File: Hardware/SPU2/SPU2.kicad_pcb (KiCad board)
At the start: 2 copper layers, 400 x 300 mm, 736 parts, among them J1 Conn_Coaxial, J2 Conn_02x13_Counter_Clockwise, J3 Conn_01x02, J4 Conn_01x04_Male, Q2 BC547, Q3 BC547, Q4 BC547, SW1 SW_Push, SW2 SW_SPDT, SW3 SW_DIP_x02, U1 74LS86, U10 74LS08, U11 74LS173, U12 74LS173, U13 74LS161, U14 74LS161, U15 74LS161, U16 74LS173, U17 74LS173, U18 NE555, U19 74LS173, U2 74LS86, U20 74LS173, U21 74LS173, U22 74LS173, U23 74LS173, U24 74LS173, U25 74LS245, U26 M84Z02, U27 M84Z02, U28 74LS245, U29 74LS00, U3 74LS245, U30 28c64, U31 28c64, U32 74LS245, U33 74LS245, U34 74LS245, U35 74LS245, U36 74LS245, U37 74LS08, U38 74HCT574, U39 74HCT574, U4 74LS283, U40 74LS161, U41 74LS04, U42 74LS08, U43 NE555, U44 NE555, U45 74HCT574, U46 74HCT574, U47 74HCT574, U48 74HCT574, U49 74HCT574, U5 74LS283, U50 74HCT574, U51 74HCT574, U52 74HCT574, U53 74HCT574, U54 74HCT574, U55 74HCT574, U56 74HCT574, U57 74HCT574, U58 74HCT574, U59 74HCT574, U6 4077, U60 74HCT574, U61 INTEL2716, U62 74LS08, U63 INTEL2716, U64 74LS08, U65 74LS08, U66 74LS08, U67 74LS08, U68 INTEL2716, U69 CD4514B, U7 4077, U70 74LS157, U71 74LS245, U72 74LS245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

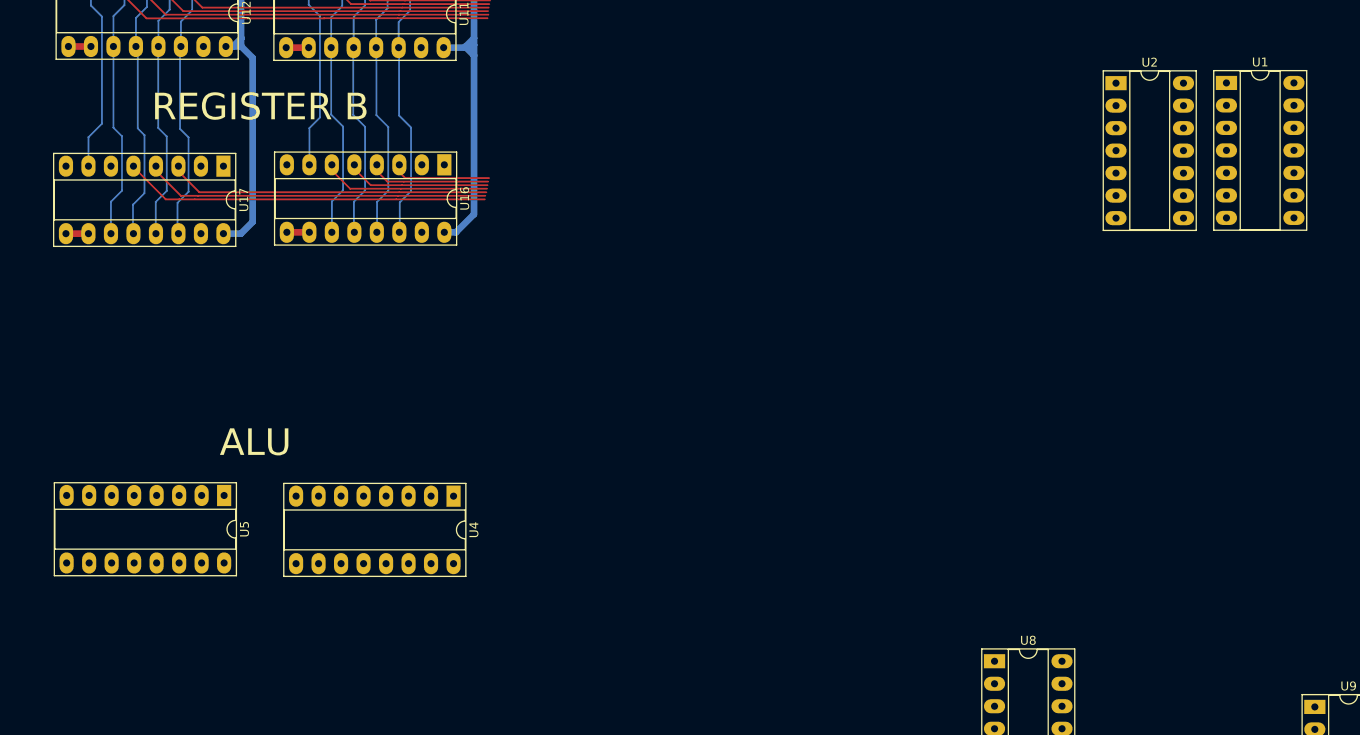
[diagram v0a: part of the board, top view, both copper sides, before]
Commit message: added subtraction to Reg B
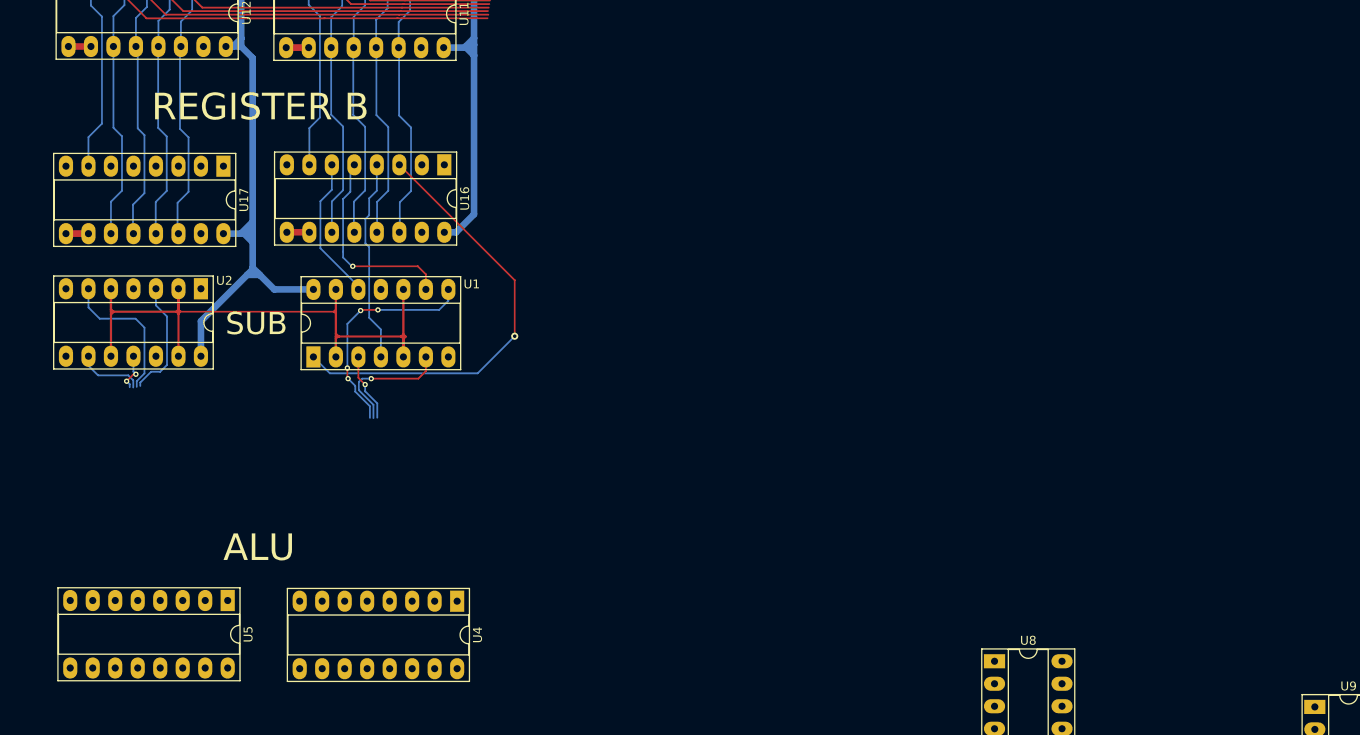
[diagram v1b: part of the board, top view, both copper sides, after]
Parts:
- moved U1 107.6 mm to (162.2, 201.0), turned to 90 degrees
- moved U2 105.9 mm to (149.5, 193.3), turned to 270 degrees
- moved U5 11.9 mm to (152.6, 228.5)
- moved U4 11.9 mm to (178.5, 228.6)
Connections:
- U1 pad 1: /REGB7 -> /REGB0
- U1 pad 11: /BAI1 -> /BAI3
- U1 pad 12: /REGB1 -> /REGB3
- U1 pad 3: /BAI7 -> /BAI0
- U1 pad 4: /REGB5 -> /REGB1
- U1 pad 6: /BAI5 -> /BAI1
- U1 pad 8: /BAI3 -> /BAI2
- U1 pad 9: /REGB3 -> /REGB2
- U2 pad 1: /REGB6 -> /REGB4
- U2 pad 11: /BAI0 -> /BAI7
- U2 pad 12: /REGB0 -> /REGB7
- U2 pad 3: /BAI6 -> /BAI4
- U2 pad 4: /REGB4 -> /REGB5
- U2 pad 6: /BAI4 -> /BAI5
- U2 pad 8: /BAI2 -> /BAI6
- U2 pad 9: /REGB2 -> /REGB6
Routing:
- net SU: track 0.00 -> 78.7 mm
- net /REGB5: track 38.9 -> 0.00 mm
- net /REGB0: track 11.2 -> 50.0 mm, vias 0 -> 1
- net /REGB4: track 36.5 -> 0.00 mm
- net /REGB6: track 41.3 -> 7.62 mm
- net +5V: track 1964.9 -> 1995.4 mm
- net /BAI2: track 0.00 -> 25.4 mm, vias 0 -> 4
- net /BAI5: track 0.00 -> 16.4 mm
- net /BAI1: track 0.00 -> 14.4 mm, vias 0 -> 1
- net /BAI4: track 0.00 -> 13.3 mm
- net /REGB1: track 13.8 -> 23.0 mm
- net /BAI0: track 0.00 -> 7.74 mm, vias 0 -> 1
- net /REGB2: track 16.3 -> 22.8 mm, vias 0 -> 1
- net /BAI7: track 0.00 -> 4.36 mm, vias 0 -> 2
- net /REGB3: track 19.0 -> 16.4 mm
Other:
- board text added: "SUB"

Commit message: schule aus
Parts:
- moved U4 15.5 mm to (177.5, 213.2)
- moved U5 15.4 mm to (152.3, 213.2)
- moved U1 0.36 mm to (161.9, 201.0)
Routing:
- net /RA5: track 39.2 -> 95.6 mm
- net /RA4: track 36.6 -> 91.8 mm
- net /RA6: track 41.9 -> 93.1 mm
- net /RA7: track 44.5 -> 86.5 mm
- net /RA3: track 19.2 -> 60.5 mm
- net SU: track 78.7 -> 115.9 mm
- net /BAI3: track 0.00 -> 33.5 mm, vias 0 -> 4
- net /BAI6: track 0.00 -> 32.9 mm, vias 0 -> 1
- net ~BI: track 5.08 -> 31.1 mm
- net /REGB7: track 0.00 -> 24.9 mm, vias 0 -> 2
- net /BAI2: track 25.4 -> 47.2 mm, vias 4 -> 5
- net /REGB6: track 7.62 -> 25.8 mm
- net /BAI7: track 4.36 -> 20.8 mm, vias 2 -> 0
- net /REGB4: track 0.00 -> 15.9 mm
- net /RA0: track 11.2 -> 26.7 mm, vias 0 -> 1
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
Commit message: began clusterfuck
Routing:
- net /RA1: track 26.9 -> 60.3 mm
- net /RA2: track 27.5 -> 60.7 mm
- net /RA0: track 26.7 -> 59.8 mm
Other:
- board size 400 x 300 mm -> 624.6 x 303.9 mm
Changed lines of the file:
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@@
-(kicad_pcb (version 20171130) (host pcbnew "(5.1.6)-1")
+(kicad_pcb (version 20171130) (host pcbnew "(5.1.4)-1")
   (general
     (thickness 1.6)
-    (drawings 27)
-    (tracks 5190)
+    (drawings 33)
+    (tracks 5200)
     (zones 0)
     (modules 736)
@@
   )
   (setup
-    (last_trace_width 0.2)
+    (last_trace_width 0.25)
     (user_trace_width 0.2)
     (user_trace_width 0.5)
@@
     )
   )
+  (gr_line (start 450.46 25.55) (end 458.1 21.88) (layer Edge.Cuts) (width 0.05))
+  (gr_line (start 445.36 294.77) (end 450.46 25.55) (layer Edge.Cuts) (width 0.05))
+  (gr_line (start 614.64 290.1) (end 445.36 294.77) (layer Edge.Cuts) (width 0.05))
+  (gr_line (start 664.61 177.34) (end 614.64 290.1) (layer Edge.Cuts) (width 0.05))
+  (gr_line (start 575.89 16.09) (end 664.61 177.34) (layer Edge.Cuts) (width 0.05))
+  (gr_line (start 458.1 21.88) (end 575.89 16.09) (layer Edge.Cuts) (width 0.05))
   (gr_text "SUB\n" (at 155.8036 196.9262) (layer F.SilkS)
     (effects (font (size 2.5 2.5) (thickness 0.3)))
@@
   (segment (start 171.8564 158.496) (end 171.8564 161.7726) (width 0.2) (layer B.Cu) (net 308))
   (segment (start 171.8564 161.7726) (end 171.0944 162.5346) (width 0.2) (layer B.Cu) (net 308))
-  (segment (start 171.0944 162.5346) (end 169.91993 163.70907) (width 0.2) (layer F.Cu) (net 308))
-  (segment (start 169.91993 163.70907) (end 169.9006 163.7284) (width 0.2) (layer F.Cu) (net 308))
+  (segment (start 137.54907 163.70907) (end 137.11 163.70907) (width 0.2) (layer F.Cu) (net 308))
+  (segment (start 160.48327 163.70907) (end 137.54907 163.70907) (width 0.2) (layer F.Cu) (net 308))
+  (segment (start 160.5026 163.7284) (end 160.48327 163.70907) (width 0.2) (layer F.Cu) (net 308))
+  (segment (start 171.0944 162.5346) (end 169.9006 163.7284) (width 0.2) (layer F.Cu) (net 308))
   (segment (start 169.9006 163.7284) (end 160.5026 163.7284) (width 0.2) (layer F.Cu) (net 308))
+  (segment (start 137.11 163.70907) (end 131.690418 163.70907) (width 0.2) (layer F.Cu) (net 308))
+  (segment (start 131.690418 163.70907) (end 128.885671 166.513817) (width 0.2) (layer F.Cu) (net 308))
+  (segment (start 128.885671 166.513817) (end 128.885671 166.84) (width 0.2) (layer F.Cu) (net 308))
   (segment (start 169.3164 158.496) (end 169.3164 159.1818) (width 0.2) (layer F.Cu) (net 309))
   (segment (start 169.3164 159.1818) (end 170.530611 160.396011) (width 0.2) (layer F.Cu) (net 309))
@@
   (segment (start 168.402 162.4584) (end 167.55134 163.30906) (width 0.2) (layer F.Cu) (net 309))
   (segment (start 167.55134 163.30906) (end 160.18534 163.30906) (width 0.2) (layer F.Cu) (net 309))
+  (segment (start 160.18534 163.30906) (end 131.52473 163.30906) (width 0.2) (layer F.Cu) (net 309))
+  (segment (start 131.52473 163.30906) (end 128.485661 166.348129) (width 0.2) (layer F.Cu) (net 309))
+  (segment (start 128.485661 166.348129) (end 128.485661 166.77) (width 0.2) (layer F.Cu) (net 309))
   (segment (start 166.7764 158.496) (end 166.7764 158.9278) (width 0.2) (layer F.Cu) (net 310))
   (segment (start 168.644621 160.796021) (end 172.567823 160.796021) (width 0.2) (layer F.Cu) (net 310))
   (segment (start 166.7764 158.9278) (end 168.644621 160.796021) (width 0.2) (layer F.Cu) (net 310))
   (segment (start 172.567823 160.796021) (end 182.1688 160.796021) (width 0.2) (layer F.Cu) (net 310))
-  (via (at 165.8366 162.306) (size 0.6) (drill 0.3) (layers F.Cu B.Cu) (net 310))
   (segment (start 166.7764 158.496) (end 166.7764 161.3662) (width 0.2) (layer B.Cu) (net 310))
   (segment (start 166.7764 161.3662) (end 165.8366 162.306) (width 0.2) (layer B.Cu) (net 310))
+  (via (at 165.8366 162.306) (size 0.6) (drill 0.3) (layers F.Cu B.Cu) (net 310))
   (segment (start 165.8366 162.306) (end 165.23355 162.90905) (width 0.2) (layer F.Cu) (net 310))
-  (segment (start 165.23355 162.90905) (end 161.786049 162.90905) (width 0.2) (layer F.Cu) (net 310))
-  (segment (start 161.786049 162.90905) (end 159.3342 162.90905) (width 0.2) (layer F.Cu) (net 310))
+  (segment (start 165.23355 162.90905) (end 131.54 162.90905) (width 0.2) (layer F.Cu) (net 310))
+  (segment (start 131.54 162.90905) (end 131.359042 162.90905) (width 0.2) (layer F.Cu) (net 310))
+  (segment (start 131.359042 162.90905) (end 128.085651 166.182441) (width 0.2) (layer F.Cu) (net 310))
+  (segment (start 128.085651 166.182441) (end 128.085651 166.71) (width 0.2) (layer F.Cu) (net 310))
   (segment (start 164.2364 158.496) (end 164.2364 158.9532) (width 0.2) (layer F.Cu) (net 311))
   (segment (start 166.479231 161.196031) (end 172.402134 161.196031) (width 0.2) (layer F.Cu) (net 311))
@@
   (segment (start 129.375489 217.506589) (end 145.348189 217.506589) (width 0.2) (layer F.Cu) (net 314))
   (segment (start 142.1384 218.4146) (end 142.1384 220.7768) (width 0.2) (layer F.Cu) (net 315))
+  (segment (start 139.6492 160.1408) (end 138.881 160.909) (width 0.2) (layer F.Cu) (net 315))
+  (segment (start 139.6492 158.369) (end 139.6492 160.1408) (width 0.2) (layer F.Cu) (net 315))
   (segment (start 141.6304 217.9066) (end 142.1384 218.4146) (width 0.2) (layer F.Cu) (net 315))
+  (segment (start 138.881 160.909) (end 130.5306 160.909) (width 0.2) (layer F.Cu) (net 315))
+  (segment (start 130.5306 160.909) (end 126.0856 165.354) (width 0.2) (layer F.Cu) (net 315))
   (segment (start 129.2098 217.9066) (end 141.6304 217.9066) (width 0.2) (layer F.Cu) (net 315))
   (segment (start 126.0856 165.354) (end 126.0856 214.7824) (width 0.2) (layer F.Cu) (net 315))
-  (segment (start 130.5306 160.909) (end 126.0856 165.354) (width 0.2) (layer F.Cu) (net 315))
-  (segment (start 138.3538 160.909) (end 130.5306 160.909) (width 0.2) (layer F.Cu) (net 315))
-  (segment (start 139.6492 159.6136) (end 138.3538 160.909) (width 0.2) (layer F.Cu) (net 315))
   (segment (start 126.0856 214.7824) (end 129.2098 217.9066) (width 0.2) (layer F.Cu) (net 315))
-  (segment (start 139.6492 158.369) (end 139.6492 159.6136) (width 0.2) (layer F.Cu) (net 315))
   (segment (start 162.2298 201.041) (end 164.084 202.8952) (width 0.2) (layer B.Cu) (net 324))
   (segment (start 164.084 202.8952) (end 177.375085 202.8952) (width 0.2) (layer B.Cu) (net 324))
